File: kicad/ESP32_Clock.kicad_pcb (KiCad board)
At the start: 2 copper layers, 100.1 x 100.1 mm, 120 parts, among them J1 Battery, J10 OLED, J12 FTDI, J2 LEDs, J3 PWR, J4 Grove 1, J5 Grove 2, J6 Grove 3, J7 Grove 4, J8 USB_OTG, J9 Gesture, Q1 NXP2301P, Q2 BCM857, Q3 UMH3N, SW1 Reset, SW2 Program, U1 MCP73831, U10 WS2812B, U11 WS2812B, U12 WS2812B, U13 WS2812B, U14 WS2812B, U15 WS2812B, U16 WS2812B, U17 WS2812B, U18 WS2812B, U19 WS2812B, U2 ESP32-WROOM, U20 WS2812B, U21 WS2812B, U22 WS2812B, U23 WS2812B, U24 WS2812B, U25 WS2812B, U26 WS2812B, U27 WS2812B, U28 WS2812B, U29 WS2812B, U3 BA33DD0WHFP, U30 WS2812B, U31 WS2812B, U32 WS2812B, U33 WS2812B, U34 APDS-9960, U35 MMA8452Q, U4 CP2104, U5 WS2812B, U6 WS2812B, U7 WS2812B, U8 WS2812B, U9 WS2812B

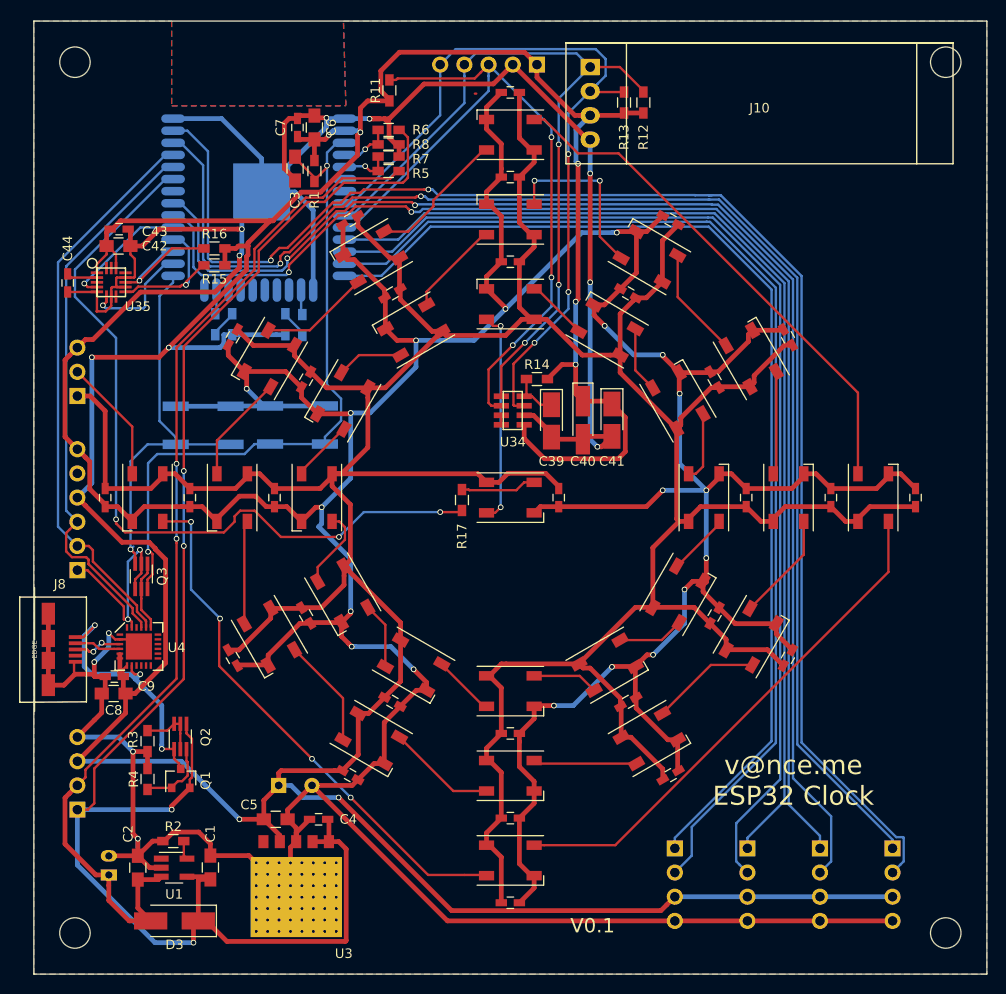
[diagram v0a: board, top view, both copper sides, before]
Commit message: PCB at v0.1, and some simple modifications to AWS IOT code using the esp-idf framework
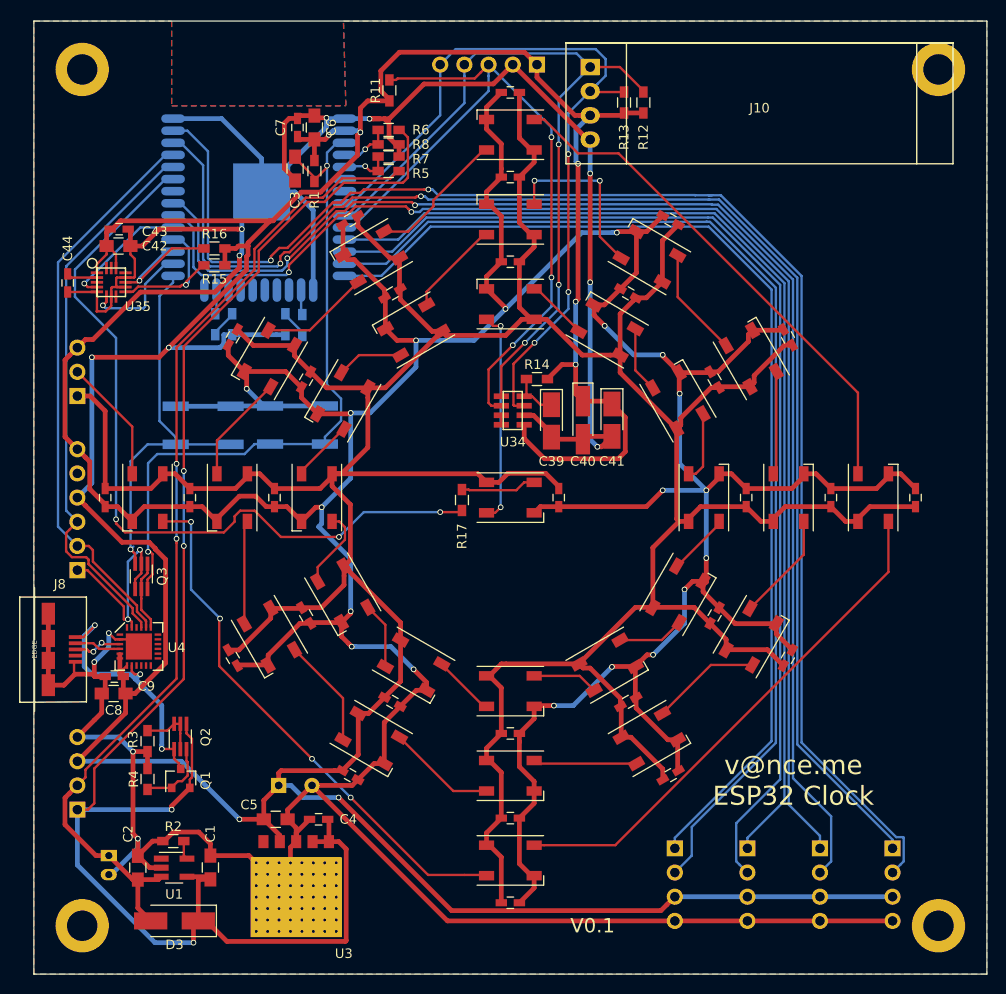
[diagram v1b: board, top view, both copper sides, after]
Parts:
- removed the REF** at (147.3, 121.9)
- removed the REF** at (147.3, 30.5)
- removed the REF** at (55.9, 30.5)
- removed the REF** at (55.9, 121.9)
- added REF**: MountingHole_3.2mm_M3_DIN965_Pad, Mounting_Holes:MountingHole_3.2mm_M3_DIN965_Pad, F.Cu at (146.6, 31.2)
- added REF**: MountingHole_3.2mm_M3_DIN965_Pad, Mounting_Holes:MountingHole_3.2mm_M3_DIN965_Pad, F.Cu at (146.6, 121.2)
- added REF**: MountingHole_3.2mm_M3_DIN965_Pad, Mounting_Holes:MountingHole_3.2mm_M3_DIN965_Pad, F.Cu at (56.6, 121.2)
- added REF**: MountingHole_3.2mm_M3_DIN965_Pad, Mounting_Holes:MountingHole_3.2mm_M3_DIN965_Pad, F.Cu at (56.6, 31.2)
- moved J1 2.03 mm to (59.4, 113.8), turned to 270 degrees
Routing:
- net VBAT: track 110.7 -> 104.8 mm
- net GND: track 840.9 -> 843.0 mm

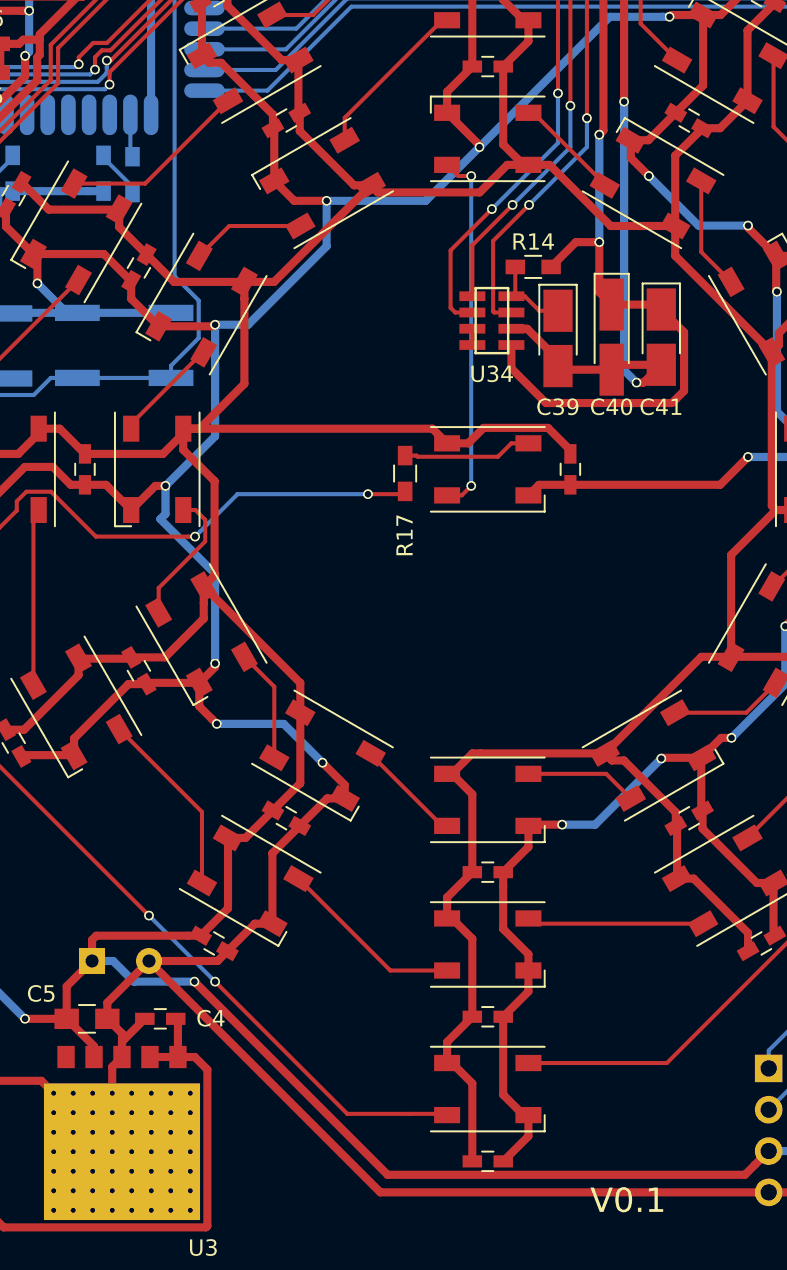
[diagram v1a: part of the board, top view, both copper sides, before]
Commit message: Initial changes after first board test
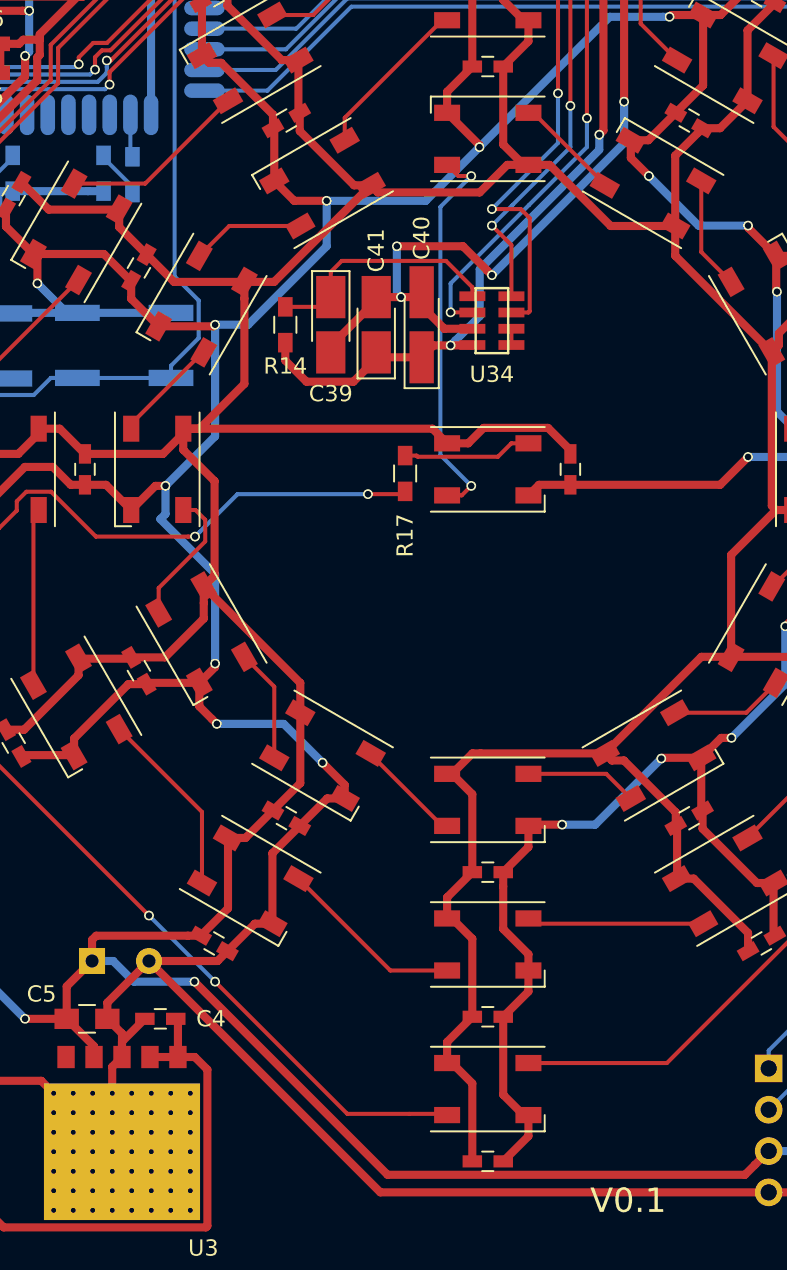
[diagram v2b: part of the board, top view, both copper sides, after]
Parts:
- moved C41 17.5 mm to (94.7, 67.3), turned to 90 degrees
- moved R14 15.6 mm to (89.2, 67.3), turned to 90 degrees
- moved C39 14.0 mm to (91.9, 67.3)
- moved C40 11.7 mm to (97.5, 67.3), turned to 90 degrees
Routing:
- net Net-(C39-Pad1): track 5.14 -> 14.8 mm
- net GND: track 843.0 -> 848.7 mm, vias 30 -> 32
- net +3V3: track 756.1 -> 751.1 mm
- net Net-(U32-Pad4): track 22.5 -> 24.1 mm
- net IO32: track 82.8 -> 84.1 mm
- net IO25: track 77.4 -> 78.2 mm

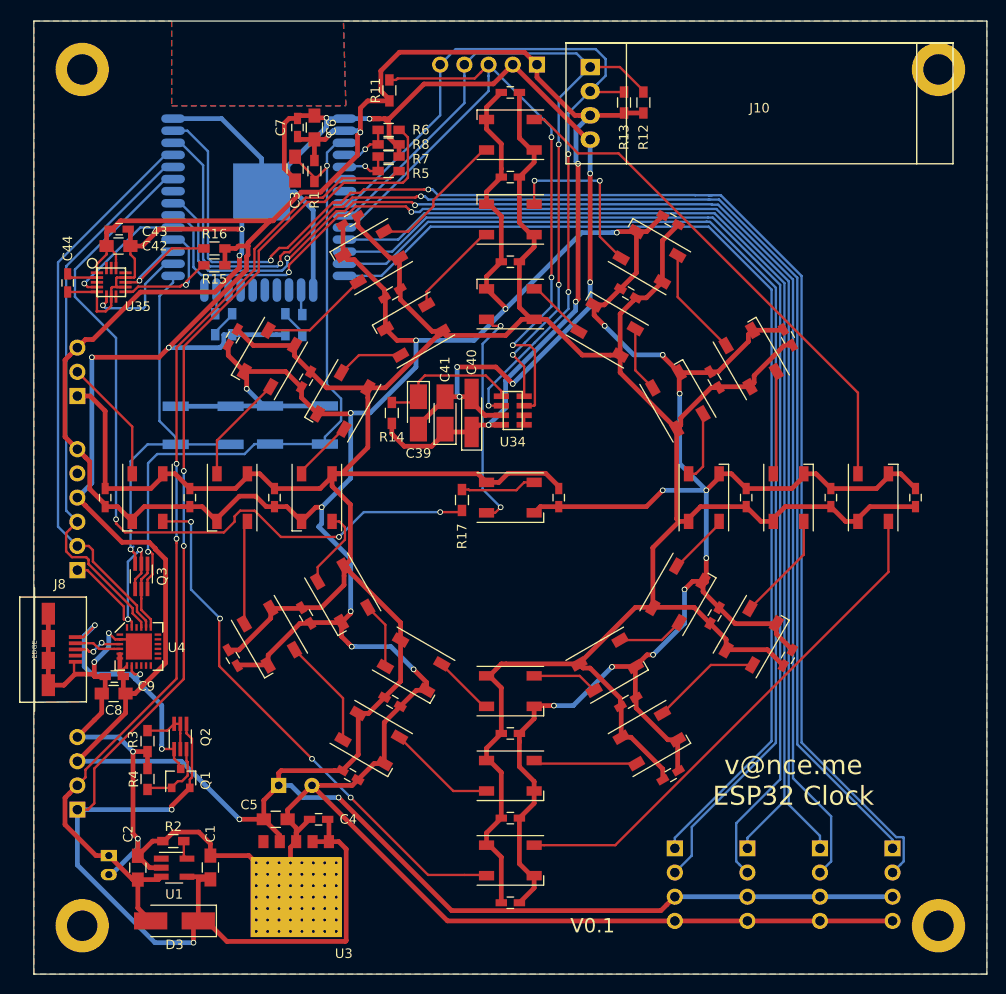
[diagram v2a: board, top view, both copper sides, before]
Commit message: Updated hardware design and removed test idf-code
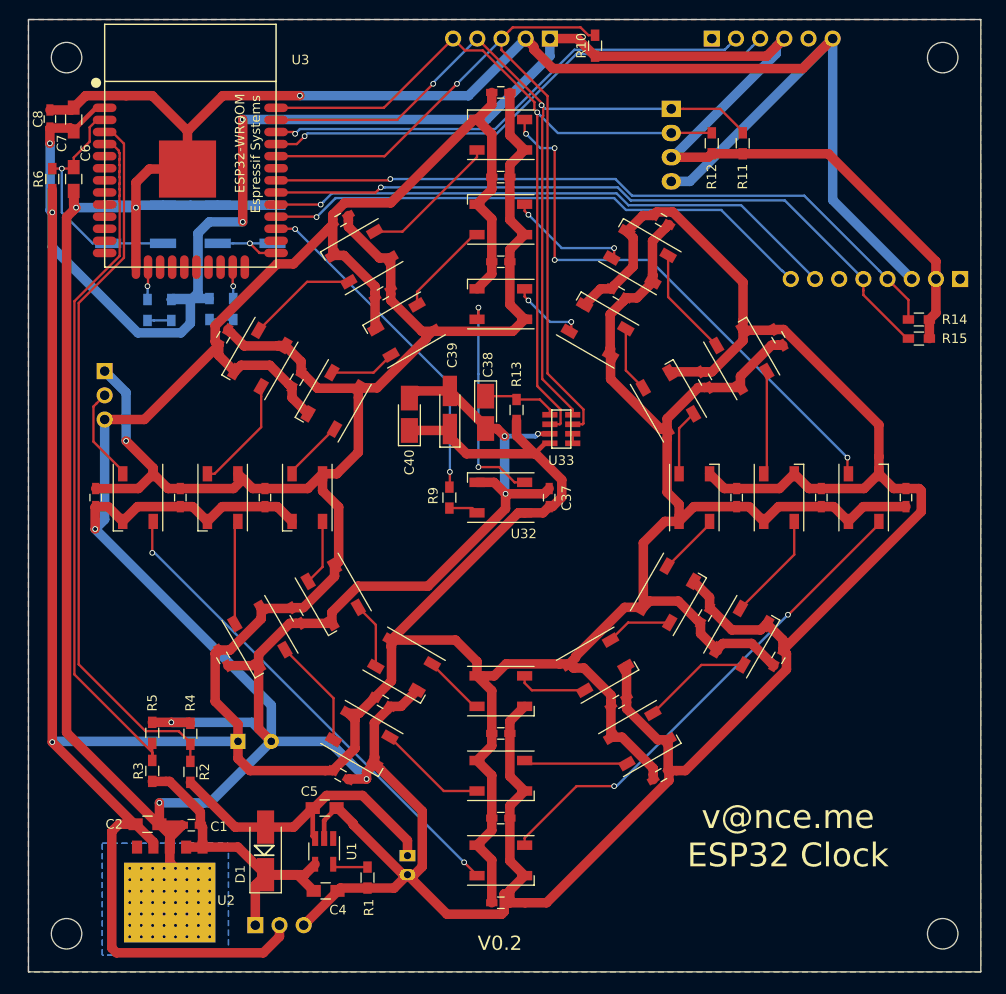
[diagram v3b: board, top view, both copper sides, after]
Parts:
- removed C41: 1uF, Capacitors_Tantalum_SMD:CP_Tantalum_Case-R_EIA-2012-12_Hand
- removed C42: 4.7uF, Capacitors_SMD:C_0805_HandSoldering
- removed C43, C44: 0.1uF, Capacitors_SMD:C_0603_HandSoldering
- removed C45: CP, Capacitors_THT:CP_Radial_D8.0mm_P3.50mm
- removed J12: FTDI, Pin_Headers:Pin_Header_Straight_1x06_Pitch2.54mm
- removed J5: Grove 2, Pin_Headers:Pin_Header_Straight_1x04_Pitch2.54mm
- removed J6: Grove 3, Pin_Headers:Pin_Header_Straight_1x04_Pitch2.54mm
- removed J7: Grove 4, Pin_Headers:Pin_Header_Straight_1x04_Pitch2.54mm
- removed J8: USB_OTG, MicroUSB_Custom:MicroUSB
- removed Q1: NXP2301P, TO_SOT_Packages_SMD:SOT-23
- removed Q2: BCM857, TO_SOT_Packages_SMD:SOT-363_SC-70-6_Handsoldering
- removed Q3: UMH3N, TO_SOT_Packages_SMD:SOT-363_SC-70-6_Handsoldering
- removed R16: 4k7, Resistors_SMD:R_0603_HandSoldering
- removed R17: 100R, Resistors_SMD:R_0603_HandSoldering
- removed the REF** at (146.6, 31.2)
- removed the REF** at (146.6, 121.2)
- removed the REF** at (56.6, 121.2)
- removed the REF** at (56.6, 31.2)
- removed U34: APDS-9960, ADPS-9960:ADPS-9960
- removed U35: MMA8452Q, QFN16:QFN-16
- added J11: MMA8542Q Accelerometer, Pin_Headers:Pin_Header_Straight_1x08_Pitch2.54mm, B.Cu at (148.8, 53.2)
- added REF**: MountingHole_3.2mm_M3, Mounting_Holes:MountingHole_3.2mm_M3, F.Cu at (147.0, 122.0)
- added REF**: MountingHole_3.2mm_M3, Mounting_Holes:MountingHole_3.2mm_M3, F.Cu at (55.0, 122.0)
- added REF**: MountingHole_3.2mm_M3, Mounting_Holes:MountingHole_3.2mm_M3, F.Cu at (55.0, 30.0)
- added REF**: MountingHole_3.2mm_M3, Mounting_Holes:MountingHole_3.2mm_M3, F.Cu at (147.0, 30.0)
- C1: value 4.7uF -> 100nF; footprint Capacitors_SMD:C_0805_HandSoldering -> Capacitors_SMD:C_0603_HandSoldering
- C2: value 4.7uF -> 10uF
- C3: value 1uF -> CP; footprint Capacitors_SMD:C_0805_HandSoldering -> Capacitors_THT:CP_Radial_D8.0mm_P3.50mm; moved to B.Cu
- C38: value 0.1uF -> 1uF; footprint Capacitors_SMD:C_0603_HandSoldering -> Capacitors_Tantalum_SMD:CP_Tantalum_Case-R_EIA-2012-12_Hand
- C39: value 1uF -> 47uF; footprint Capacitors_Tantalum_SMD:CP_Tantalum_Case-R_EIA-2012-12_Hand -> Capacitors_Tantalum_SMD:CP_Tantalum_Case-A_EIA-3216-18_Hand
- C4: value 100nF -> 4.7uF; footprint Capacitors_SMD:C_0603_HandSoldering -> Capacitors_SMD:C_0805_HandSoldering
- C40: value 47uF -> 1uF; footprint Capacitors_Tantalum_SMD:CP_Tantalum_Case-A_EIA-3216-18_Hand -> Capacitors_Tantalum_SMD:CP_Tantalum_Case-R_EIA-2012-12_Hand
- C5: value 10uF -> 4.7uF
- C6: value 10uF -> 1uF
- C7: value 100nF -> 10uF; footprint Capacitors_SMD:C_0603_HandSoldering -> Capacitors_SMD:C_0805_HandSoldering
- C8: value 10uF -> 100nF; footprint Capacitors_SMD:C_0805_HandSoldering -> Capacitors_SMD:C_0603_HandSoldering
- C9: value 100nF -> 0.1uF
- D1: value LED -> (none); footprint LEDs:LED_0603_HandSoldering -> Diodes_SMD:D_SMA_Handsoldering; moved to F.Cu
- D3: value (none) -> LED; footprint Diodes_SMD:D_SMA_Handsoldering -> LEDs:LED_0603_HandSoldering; moved to B.Cu
- J1: value Battery -> Pwr; footprint Connectors_JST:JST_PH_S2B-PH-K_02x2.00mm_Angled -> Pin_Headers:Pin_Header_Straight_1x03_Pitch2.54mm
- J10: moved to B.Cu
- J2: value LEDs -> Battery; footprint Pin_Headers:Pin_Header_Straight_1x03_Pitch2.54mm -> Connectors_JST:JST_PH_S2B-PH-K_02x2.00mm_Angled
- J3: value PWR -> FTDI; footprint Pin_Headers:Pin_Header_Straight_1x04_Pitch2.54mm -> Pin_Headers:Pin_Header_Straight_1x06_Pitch2.54mm
- J4: value Grove 1 -> LEDs; footprint Pin_Headers:Pin_Header_Straight_1x04_Pitch2.54mm -> Pin_Headers:Pin_Header_Straight_1x03_Pitch2.54mm
- R1: value 10k -> 2k
- R10: value 1k -> 10k; moved to F.Cu
- R11, R3: value 10k -> 4k7
- R13: value 4k7 -> 22R
- R14: value 22R -> 4k7
- R2: value 2k -> 4k7
- R4: value 47k -> 4k7
- R6: value 4k7 -> 10k
- R7, R8: value 4k7 -> 1k; moved to B.Cu
- R9: value 1k -> 100R; moved to F.Cu
- U2: value ESP32-WROOM -> BA33DD0WHFP; footprint ESP32-footprints-Lib:ESP32-WROOM -> LDO:LDO; moved to F.Cu
- U3: value BA33DD0WHFP -> ESP32-WROOM; footprint LDO:LDO -> ESP32-footprints-Lib:ESP32-WROOM
- U33: value WS2812B -> APDS-9960; footprint LEDs:LED_WS2812B-PLCC4 -> ADPS-9960:ADPS-9960
- U4: value CP2104 -> WS2812B; footprint QFN-24:QFN-24 -> LEDs:LED_WS2812B-PLCC4
- moved J3 104.8 mm to (122.8, 28.0), turned to 270 degrees
- moved J4 96.7 mm to (59.0, 62.9)
- moved U3 78.9 mm to (68.0, 39.2)
- moved U2 76.8 mm to (65.8, 117.9), turned to 180 degrees
- moved R1 74.4 mm to (86.6, 116.1)
- moved R15 74.4 mm to (144.5, 59.5)
- moved D3 64.5 mm to (72.5, 56.4), turned to 270 degrees
- moved R5 64.0 mm to (64.0, 100.9), turned to 90 degrees
- moved C12 60.9 mm to (100.6, 33.7), turned to 180 degrees
- moved C8 60.7 mm to (53.2, 36.5), turned to 90 degrees
- moved C3 60.4 mm to (73.0, 101.8), turned to 0 degrees
- moved C11 59.5 mm to (143.1, 76.2), turned to 90 degrees
- moved C10 59.5 mm to (100.6, 118.7), turned to 0 degrees
- moved J2 59.4 mm to (90.8, 113.8), turned to 270 degrees
- moved R14 56.2 mm to (144.5, 57.5), turned to 180 degrees
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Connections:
- C2 pad 1: VBAT -> +3V3
- C3 pad 1: EN -> +3V3
- C38 pad 1: +3V3 -> Net-(C38-Pad1)
- C39 pad 1: Net-(C39-Pad1) -> +3V3
- C5 pad 1: +3V3 -> VBAT
- C6 pad 1: +3V3 -> Net-(C6-Pad1)
- D1 pad 1: Net-(D1-Pad1) -> +5V
- D1 pad 2: Net-(D1-Pad2) -> VBAT
- D3 pad 1: +5V -> Net-(D3-Pad1)
- D3 pad 2: VBAT -> Net-(D3-Pad2)
- J1 pad 1: VBAT -> +5V
- J1 pad 2: GND -> +3V3
- J10 pad 1: IO33 -> IO22
- J10 pad 2: IO32 -> IO23
- J2 pad 1: +3V3 -> VBAT
- J2 pad 2: /LEDs/DOUT -> GND
- J3 pad 1: +5V -> Net-(J3-Pad1)
- J3 pad 2: VBAT -> TXD0
- J3 pad 3: +3V3 -> RXD0
- J3 pad 4: GND -> +3V3
- J4 pad 1: IO22 -> +3V3
- J4 pad 2: IO23 -> /LEDs/DOUT
- J4 pad 3: +3V3 -> GND
- J9 pad 3: IO25 -> IO21
- J9 pad 4: IO33 -> IO22
- J9 pad 5: IO32 -> IO23
- R1 pad 1: +3V3 -> Net-(R1-Pad1)
- R1 pad 2: EN -> GND
- R10 pad 2: Net-(D2-Pad2) -> IO21
- R11 pad 2: IO25 -> IO22
- R12 pad 2: IO33 -> IO23
- R13 pad 2: IO32 -> Net-(C38-Pad1)
- R14 pad 2: Net-(C39-Pad1) -> IO19
- R15 pad 2: IO17 -> IO18
- R2 pad 1: Net-(R2-Pad1) -> VBAT
- R2 pad 2: GND -> VP
- R3 pad 1: Net-(Q2-Pad2) -> +5V
- R3 pad 2: GND -> VN
- R4 pad 1: Net-(Q1-Pad1) -> VP
- R5 pad 1: VBAT -> VN
- R5 pad 2: VN -> GND
- R6 pad 1: +5V -> +3V3
- R6 pad 2: VP -> Net-(C6-Pad1)
- R7 pad 1: VN -> Net-(D2-Pad2)
- R7 pad 2: GND -> +3V3
- R8 pad 1: VP -> +3V3
- R8 pad 2: GND -> Net-(D3-Pad2)
- R9 pad 1: Net-(D1-Pad2) -> IO16
- R9 pad 2: +3V3 -> Net-(R9-Pad2)
- SW1 pad 1: EN -> Net-(C6-Pad1)
- SW2 pad 1: IO0 -> Net-(SW2-Pad1)
- U1 pad 5: Net-(R2-Pad1) -> Net-(R1-Pad1)
- U2 pad 1: GND -> +5V
- U2 pad 2: +3V3 -> +5V
- U2 pad 3: EN -> GND
- U2 pad 4: VP -> +3V3
- U2 pad 5: VN -> Net-(U2-Pad5)
- U3 pad 1: +5V -> GND
- U3 pad 2: +5V -> +3V3
- U3 pad 3: GND -> Net-(C6-Pad1)
- U3 pad 4: +3V3 -> VP
- U3 pad 5: Net-(U3-Pad5) -> VN
- U32 pad 4: Net-(U32-Pad4) -> Net-(R9-Pad2)
- U33 pad 1: +3V3 -> IO22
- U33 pad 2: Net-(U32-Pad4) -> IO21
- U33 pad 3: GND -> Net-(U33-Pad3)
- U33 pad 4: Net-(R17-Pad2) -> Net-(U33-Pad3)
- U4 pad 1: Net-(U4-Pad1) -> +3V3
- U4 pad 2: GND -> /LEDs/DOUT
- U4 pad 3: D+ -> GND
- U4 pad 4: D- -> Net-(U4-Pad4)
- U5 pad 2: /LEDs/DOUT -> Net-(U4-Pad4)
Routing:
- net +5V: track 175.9 -> 36.9 mm, vias 4 -> 0
- net IO14: track 115.9 -> 0.00 mm
- net IO27: track 114.3 -> 0.00 mm
- net IO12: track 112.6 -> 0.00 mm
- net IO26: track 111.3 -> 0.00 mm
- net IO32: track 84.1 -> 0.00 mm, vias 3 -> 0
- net IO33: track 81.0 -> 0.00 mm, vias 3 -> 0
- net IO25: track 78.2 -> 0.00 mm, vias 3 -> 0
- net EN: track 73.9 -> 0.00 mm, vias 2 -> 0
- net VBAT: track 104.8 -> 33.0 mm, vias 2 -> 0
- net VP: track 5.51 -> 76.3 mm, vias 1 -> 0
- net IO19: track 141.8 -> 73.8 mm, vias 2 -> 1
- net VN: track 5.30 -> 73.1 mm, vias 1 -> 0
- net IO23: track 153.8 -> 88.3 mm, vias 2 -> 1
- net IO18: track 137.5 -> 74.2 mm, vias 2 -> 1
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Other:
- board size 100.1 x 100.1 mm -> 100 x 100 mm
- net class Power: trace_width 0.5 -> 1
- board text added: "+"
- board text added: "3V3"
- board text added: "ACCEL MM8452Q"
- board text added: "FTDI"
- board text added: "Gesture ADPS-9960"
- board text added: "INT0"
- board text added: "INT1"
- board text added: "INT2"
- board text added: "PROGRAM"
- board text added: "RX"
- board text added: "SCL0"
- board text added: "SCL1"
- board text added: "SDA0"
- board text added: "SDA1"
- board text added: "TX"
- board text added: "V0.2"
- board text removed: "12"
- board text removed: "14"
- board text removed: "18"
- board text removed: "19"
- board text removed: "22"
- board text removed: "23"
- board text removed: "26"
- board text removed: "27"
- board text removed: "3.3V"
- board text removed: "APDS-9960"
- board text removed: "DTR"
- board text removed: "INT"
- board text removed: "PROG"
- board text removed: "RXDI"
- board text removed: "SCL"
- board text removed: "SDA"
- board text removed: "TXDO"
- board text removed: "V0.1"

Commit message: Added pullup to IO0 to be safe during boot
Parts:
- added R16: 10k, Resistors_SMD:R_0603_HandSoldering, B.Cu at (75.0, 56.2)
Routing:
- net +3V3: track 760.5 -> 769.2 mm
- net Net-(R16-Pad2): track 8.93 -> 14.9 mm

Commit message: Version 0.2 of the board layout - submitted for manufacture
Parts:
- removed the REF** at (147.0, 122.0)
- removed the REF** at (55.0, 122.0)
- removed the REF** at (55.0, 30.0)
- removed the REF** at (147.0, 30.0)
- added REF**: MountingHole_3.2mm_M3_Pad_Via, Mounting_Holes:MountingHole_3.2mm_M3_Pad_Via, F.Cu at (147.0, 30.0)
- added REF**: MountingHole_3.2mm_M3_Pad_Via, Mounting_Holes:MountingHole_3.2mm_M3_Pad_Via, F.Cu at (55.0, 30.0)
- added REF**: MountingHole_3.2mm_M3_Pad_Via, Mounting_Holes:MountingHole_3.2mm_M3_Pad_Via, F.Cu at (55.0, 122.0)
- added REF**: MountingHole_3.2mm_M3_Pad_Via, Mounting_Holes:MountingHole_3.2mm_M3_Pad_Via, F.Cu at (147.0, 122.0)
